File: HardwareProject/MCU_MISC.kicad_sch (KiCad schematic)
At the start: 61 parts, among them J4 Conn_ARM_JTAG_SWD_20, J5 Conn_01x03, J6 Conn_01x03, J7 SMA, J8 SMA, SW1 焊盘, SW2 Push_Button, SW3 Push_Button, SW4 Push_Button, U10 TJA1044GTK/3Z, U19 XC6206PxxxMR, U22 TMP112xxDRL, U4 HPM6P41IPB1, U6 AT24C08C-SSHM-T, U7 TMP112xxDRL, U8 TMP112xxDRL, U9 SIT3088ETK, Y1 24MHz ±10ppm 6pF

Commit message: Rev3最终版本
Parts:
- added TP5, TP6: TestPoint_Probe, HPM6P41_BB:TestPoint_Bridge_Pitch1.2mm_Drill0.7mm, symbol Connector:TestPoint_Probe
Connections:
- net 485_RX: now also TP5.1
- net 485_TX: now also TP6.1
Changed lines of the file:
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@@
 	)
 	(junction
+		(at 200.66 125.73)
+		(diameter 0)
+		(color 0 0 0 0)
+	)
+	(junction
 		(at 86.36 97.79)
 		(diameter 0)
@@
 	)
 	(junction
+		(at 200.66 115.57)
+		(diameter 0)
+		(color 0 0 0 0)
+	)
+	(junction
 		(at 78.74 138.43)
 		(diameter 0)
@@
 	(wire
 		(pts
+			(xy 200.66 127) (xy 200.66 125.73)
+		)
+		(stroke
+			(width 0)
+			(type default)
+		)
+	)
+	(wire
+		(pts
 			(xy 246.38 50.8) (xy 259.08 50.8)
 		)
@@
 	(wire
 		(pts
+			(xy 200.66 114.3) (xy 200.66 115.57)
+		)
+		(stroke
+			(width 0)
+			(type default)
+		)
+	)
+	(wire
+		(pts
 			(xy 209.55 104.14) (xy 210.82 104.14)
 		)
@@
 	)
 	(symbol
+		(lib_id "Connector:TestPoint_Probe")
+		(at 200.66 127 180)
+		(unit 1)
+		(exclude_from_sim no)
+		(in_bom yes)
+		(on_board yes)
+		(dnp no)
+		(property "Reference" "TP6"
+			(at 197.104 131.826 0)
+			(effects
+				(font
+					(size 1.27 1.27)
+				)
+				(justify right)
+			)
+		)
+		(property "Value" "TestPoint_Probe"
+			(at 196.85 127.3176 0)
+			(effects
+				(font
+					(size 1.27 1.27)
+				)
+				(justify left)
+				(hide yes)
+			)
+		)
+		(property "Footprint" "HPM6P41_BB:TestPoint_Bridge_Pitch1.2mm_Drill0.7mm"
+			(at 195.58 127 0)
+			(effects
+				(font
+					(size 1.27 1.27)
+				)
+				(hide yes)
+			)
+		)
+		(property "Datasheet" "~"
+			(at 195.58 127 0)
+			(effects
+				(font
+					(size 1.27 1.27)
+				)
+				(hide yes)
+			)
+		)
+		(property "Description" "test point (alternative probe-style design)"
+			(at 200.66 127 0)
+			(effects
+				(font
+					(size 1.27 1.27)
+				)
+				(hide yes)
+			)
+		)
+		(pin "1"
+		)
+		(instances
+			(project "HPM6P41_BB"
+				(path "/714b8a30-f9a7-49d4-a000-bc20c4884c7a/5ba70b1a-2680-42f0-98ce-27de27e994eb"
+					(reference "TP6")
+					(unit 1)
+				)
+			)
+		)
+	)
+	(symbol
 		(lib_id "power:+3.3V")
 		(at 172.72 29.21 0)
@@
 					(unit 1)
 				)
+			)
+		)
+	)
+	(symbol
+		(lib_id "Connector:TestPoint_Probe")
+		(at 200.66 114.3 90)
+		(unit 1)
+		(exclude_from_sim no)
+		(in_bom yes)
+		(on_board yes)
+		(dnp no)
+		(fields_autoplaced yes)
+		(property "Reference" "TP5"
+			(at 199.0725 109.22 90)
+			(effects
+				(font
+					(size 1.27 1.27)
+				)
+			)
+		)
+		(property "Value" "TestPoint_Probe"
+			(at 200.3424 110.49 0)
+			(effects
+				(font
+					(size 1.27 1.27)
+				)
+				(justify left)
+				(hide yes)
+			)
+		)
+		(property "Footprint" "HPM6P41_BB:TestPoint_Bridge_Pitch1.2mm_Drill0.7mm"
+			(at 200.66 109.22 0)
+			(effects
+				(font
+					(size 1.27 1.27)
+				)
+				(hide yes)
+			)
+		)
+		(property "Datasheet" "~"
+			(at 200.66 109.22 0)
+			(effects
+				(font
+					(size 1.27 1.27)
+				)
+				(hide yes)
+			)
+		)
+		(property "Description" "test point (alternative probe-style design)"
+			(at 200.66 114.3 0)
+			(effects
+				(font
+					(size 1.27 1.27)
+				)
+				(hide yes)
+			)
+		)
+		(pin "1"
+		)
+		(instances
+			(project "HPM6P41_BB"
+				(path "/714b8a30-f9a7-49d4-a000-bc20c4884c7a/5ba70b1a-2680-42f0-98ce-27de27e994eb"
+					(reference "TP5")
+					(unit 1)
+				)

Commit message: 外置核心电压SYR838以改善ADC噪声
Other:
- note added: "EEPROM JTAG TRGM 温度计"
- note removed: "USB EEPROM JTAG TRGM 温度计"
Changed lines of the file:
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@@
 		)
 	)
-	(text "USB EEPROM\nJTAG TRGM 温度计"
+	(text "EEPROM JTAG TRGM 温度计"
 		(exclude_from_sim no)
 		(at 95.504 185.42 0)

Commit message: 换其他电感之前暂存一下
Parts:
- removed C84, C85: 1uF,10V, Capacitor_SMD:C_0603_1608Metric, symbol Device:C
- removed J4: Conn_ARM_JTAG_SWD_20, Connector_IDC:IDC-Header_2x10_P2.54mm_Vertical, symbol Connector:Conn_ARM_JTAG_SWD_20
- removed TP5, TP6: TestPoint_Probe, HPM6P41_BB:TestPoint_Bridge_Pitch1.2mm_Drill0.7mm, symbol Connector:TestPoint_Probe
- removed U19: XC6206PxxxMR, Package_TO_SOT_SMD:SOT-23-3, symbol Regulator_Linear:XC6206PxxxMR
- added C100, C101: 100nF, Capacitor_SMD:C_0603_1608Metric, symbol Device:C
- added C102, C103: 4.7uF,10V, Capacitor_SMD:C_0603_1608Metric, symbol Device:C
- added U27: CA-IS3762HN, kicad_community_lib:CA-IS3762HN, symbol CA-IS3762HN:CA-IS3762HN
- added U28: TME-0505S, Converter_DCDC:Converter_DCDC_TRACO_TME_03xxS_05xxS_12xxS_Single_THT, symbol Converter_DCDC:TME-0505S
- J7, J8: footprint HPM6P41_BB:SMA_Amphenol_901-144_Vertical -> Connector_Coaxial:SMA_Amphenol_901-144_Vertical
- L2, L3: footprint 1MyFootPrint:L4532 -> HPM6P41_BB:SDCW2012-2-900TF
- U9: footprint Package_SO:SOIC-8_3.9x4.9mm_P1.27mm -> Package_SON:HVSON-8-1EP_3x3mm_P0.65mm_EP1.6x2.4mm
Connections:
- net +3.3V: now also C100.2, U27.1 (VDDA)
- net +5V: now also C102.1, U28.2 (+Vin); no longer C29.2, U10.3 (VCC)
- net 485_DE: now also U27.2 (VI1); no longer R40.2, U9.2 (~{RE}), U9.3 (DE)
- net 485_RX: now also U27.6 (VO5); no longer U9.1 (RO)
- net 485_TX: now also U27.3 (VI2); no longer U9.4 (DI)
- net CAN_RXD: now also U27.7 (VO6); no longer U10.4 (RXD)
- net CAN_STBY: now also U27.5 (VI4); no longer U10.8 (STB)
- net CAN_TXD: now also U27.4 (VI3); no longer U10.1 (TXD)
- net GND: now also C100.1, C102.2, U27.8 (GNDA), U28.1 (-Vin); no longer C27.1, C28.1, C29.1, C30.1, C31.2, C32.1, C33.2, D10.3 (A), D9.3 (A), J5.2 (Pin_2), J6.2 (Pin_2), R40.1, U10.2 (GND), U10.9 (EP), U9.5 (GND)
- net at L3.1: now also U10.6 (CANL); no longer U10.7 (CANH)
- net at L3.2: now also U10.7 (CANH); no longer U10.6 (CANL)
- net at C31.1, J5.1 (Pin_1), JP2.1 (A): now also D9.1 (K), L3.4; no longer D9.2 (K), L3.3
- net at C30.2, J5.3 (Pin_3), R42.1: now also D9.2 (K), L3.3; no longer D9.1 (K), L3.4
- net at C32.2, D10.2 (K), J6.1 (Pin_1)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: now also L2.4; no longer L2.3
- net at C33.1, D10.1 (K), J6.3 (Pin_3)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: now also L2.3; no longer L2.4
- net at L2.1: now also U9.6 (A); no longer U9.7 (B)
- net at L2.2: now also U9.7 (B); no longer U9.6 (A)
- net +3.3VC renamed +5VC
- net +5VC: now also C29.2, U10.3 (VCC), C101.2, C103.1, U27.16 (VDDB), U28.4 (+Vout)
- new net 485_DE_ISO: R40.2, U27.13 (VO3), U9.2 (~{RE}), U9.3 (DE)
- new net 485_RX_ISO: U27.10 (VI6), U9.1 (RO)
- new net 485_TX_ISO: U27.12 (VO4), U9.4 (DI)
- new net CAN_RXD_ISO: U10.4 (RXD), U27.11 (VI5)
- new net CAN_STBY_ISO: U10.8 (STB), U27.14 (VO2)
- new net CAN_TXD_ISO: U10.1 (TXD), U27.15 (VO1)
- new net ISO_GNDC: C101.1, C103.2, C27.1, C28.1, C29.1, C30.1, C31.2, C32.1, C33.2, D10.3 (A), D9.3 (A), J5.2 (Pin_2), J6.2 (Pin_2), R40.1, U10.2 (GND), U10.9 (EP), U27.9 (GNDB), U28.3 (-Vout), U9.5 (GND), U9.9 (EP)
- no-connect marks 5 -> 0
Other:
- note added: "EEPROM TRGM 温度计"
- note removed: "EEPROM JTAG TRGM 温度计"
- moved on the sheet: C23, C24, C26, C88, J7, J8, JP1, R35, R36, R38, R39, R49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

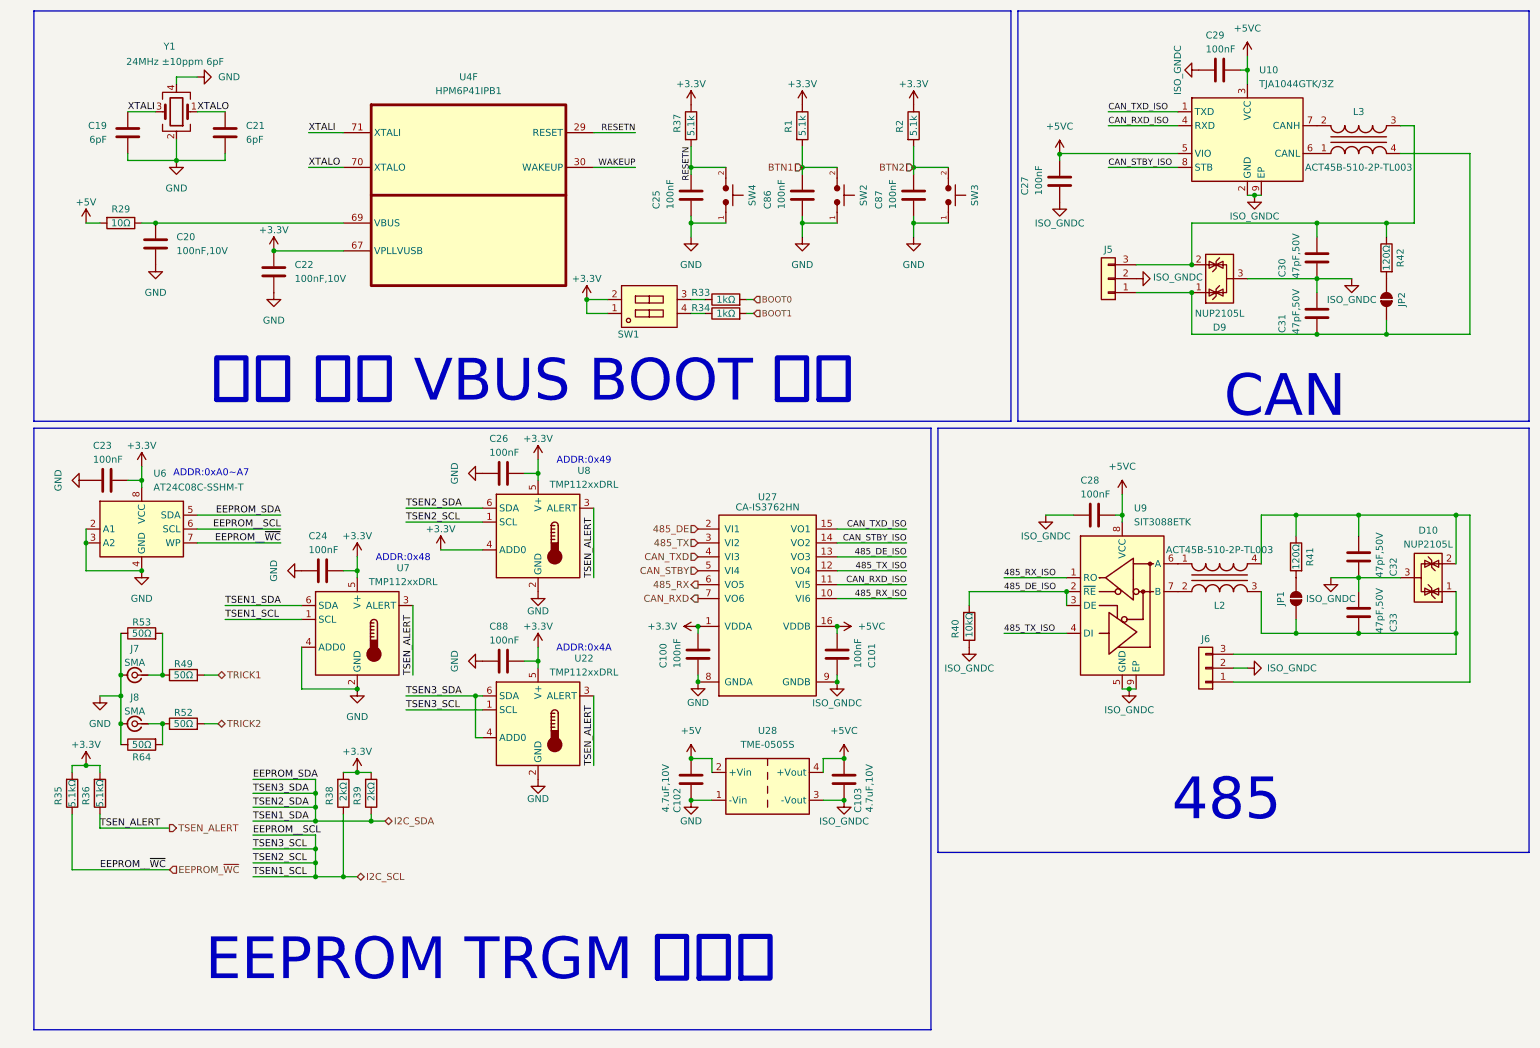
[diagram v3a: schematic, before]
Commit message: 完成Rev4 电源 驱动 模拟 IO
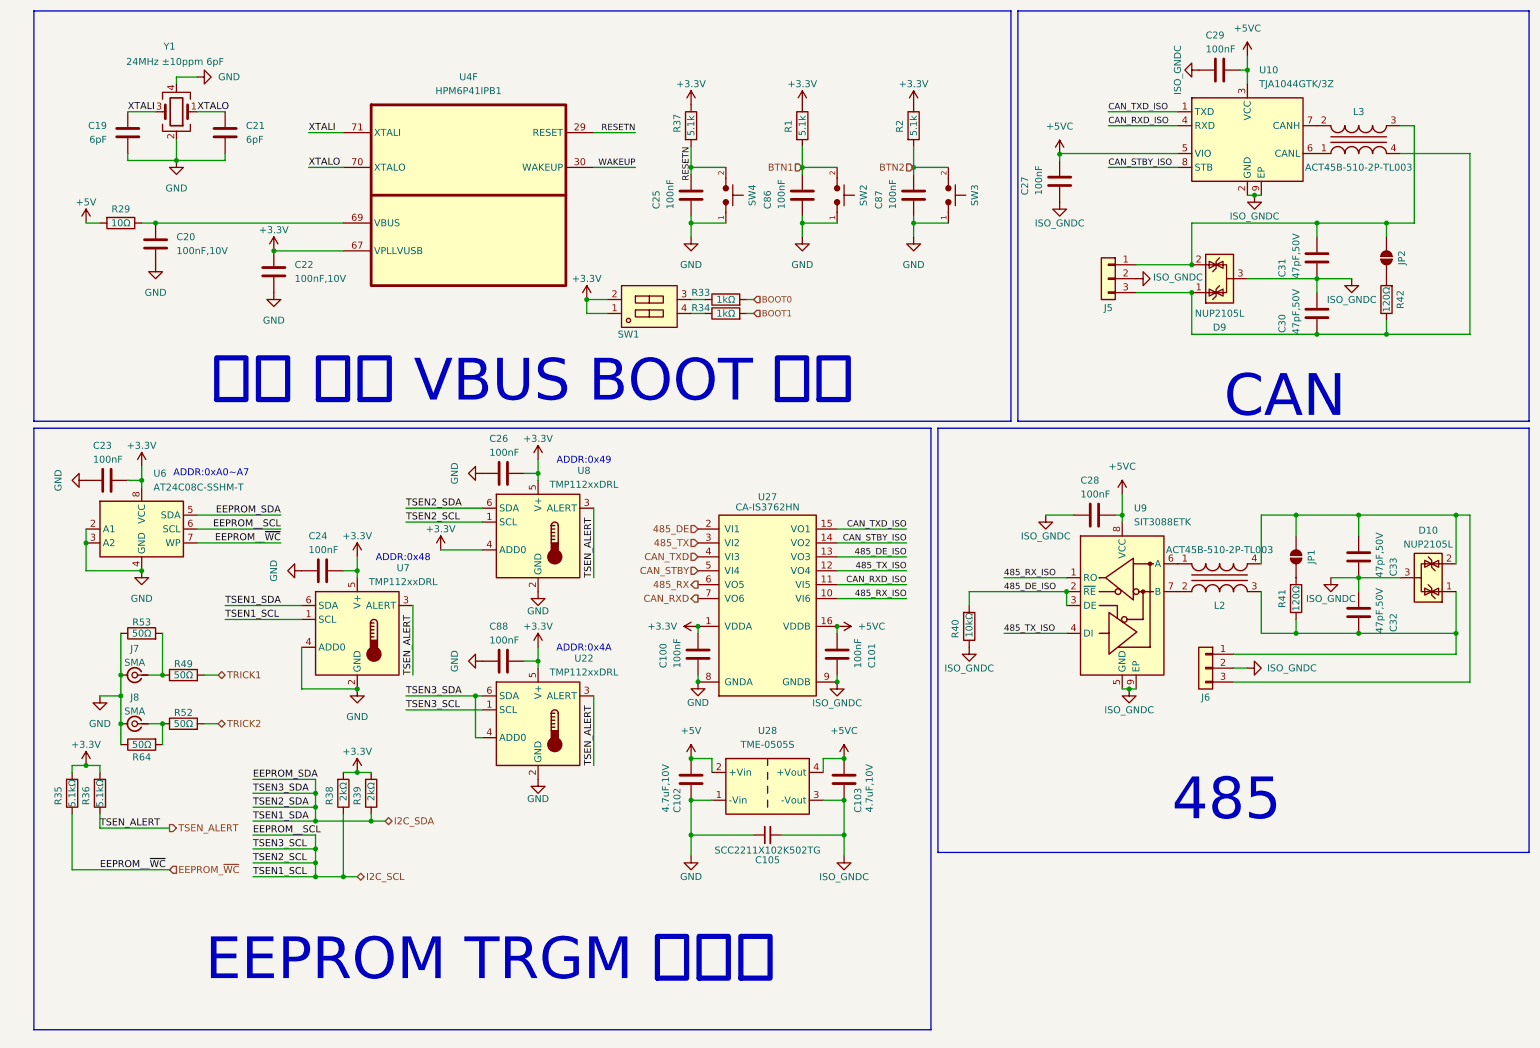
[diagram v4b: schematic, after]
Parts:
- added C105: SCC2211X102K502TG, kicad_community_lib:SCC2211X102K502T, symbol SCC2211X102K502T:SCC2211X102K502T
- J7, J8: footprint Connector_Coaxial:SMA_Amphenol_901-144_Vertical -> HPM6P41_BB:SMA_Amphenol_901-144_Vertical
- U28: footprint Converter_DCDC:Converter_DCDC_TRACO_TME_03xxS_05xxS_12xxS_Single_THT -> HPM6P41_BB:BXXXXS-1W隔离电源
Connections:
- net GND: now also C105.1
- net ISO_GNDC: now also C30.2, C31.1, C32.2, C33.1, C105.2; no longer C30.1, C31.2, C32.1, C33.2
- new net: C31.2, D9.2 (K), J5.1 (Pin_1), JP2.1 (A), L3.3
- new net: C30.1, D9.1 (K), J5.3 (Pin_3), L3.4, R42.1
- new net: C32.1, D10.1 (K), J6.1 (Pin_1), L2.3, R41.1
- new net: C33.2, D10.2 (K), J6.3 (Pin_3), JP1.1 (A), L2.4
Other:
- moved on the sheet: C30, C31, C32, C33, J5, J6, JP1, JP2, R41, R42

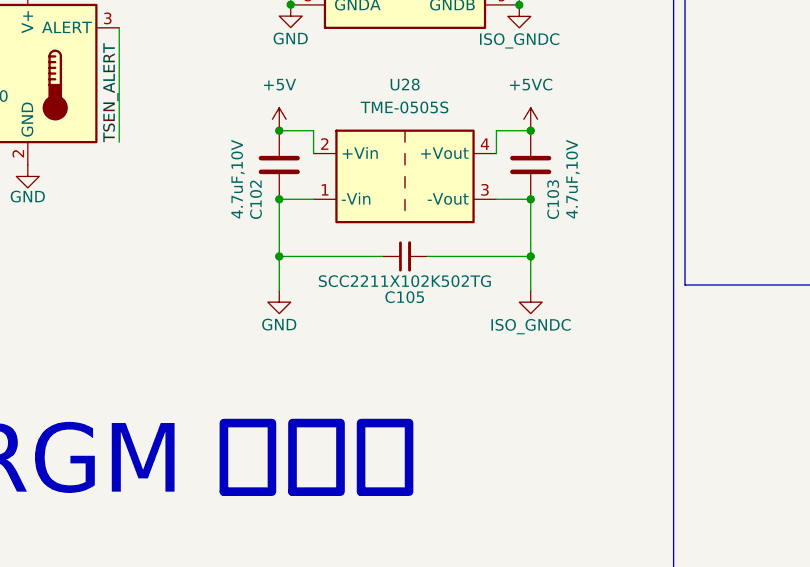
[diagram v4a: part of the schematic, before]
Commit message: 更新readme暂停通知，添加测试用例源代码
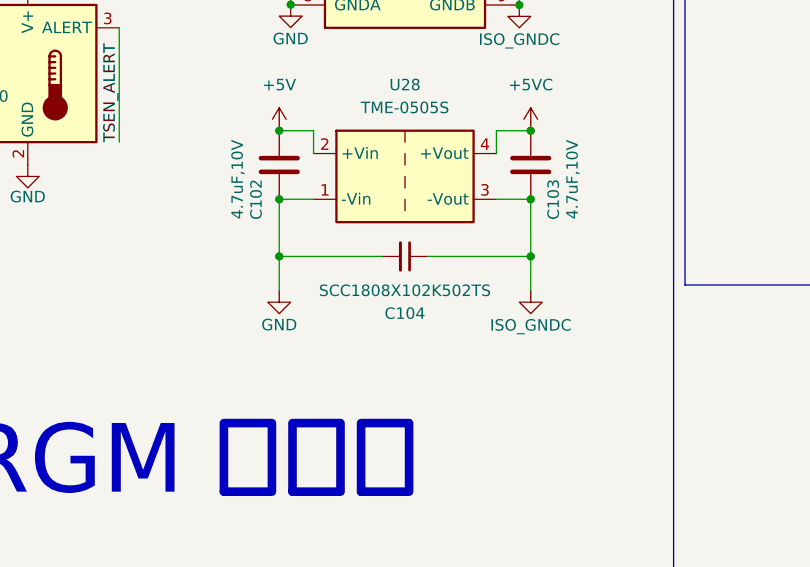
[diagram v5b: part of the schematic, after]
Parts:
- removed C105: SCC2211X102K502TG, kicad_community_lib:SCC2211X102K502T, symbol SCC2211X102K502T:SCC2211X102K502T
- added C104: SCC1808X102K502TS, Capacitor_SMD:C_1808_4520Metric, symbol SCC1808X102K502TS:SCC1808X102K502TS
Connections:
- net GND: now also C104.2
- net ISO_GNDC: now also C104.1
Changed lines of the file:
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@@
+	)
+	(symbol
+		(lib_id "SCC1808X102K502TS:SCC1808X102K502TS")
+		(at 146.05 162.56 270)
+		(mirror x)
+		(unit 1)
+		(exclude_from_sim no)
+		(in_bom yes)
+		(on_board yes)
+		(dnp no)
+		(property "Reference" "C104"
+			(at 146.0436 168.91 90)
+			(effects
+				(font
+					(size 1.27 1.27)
+				)
+			)
+		)
+		(property "Value" "SCC1808X102K502TS"
+			(at 146.0436 166.37 90)
+			(effects
+				(font
+					(size 1.27 1.27)
+				)
+			)
+		)
+		(property "Footprint" "Capacitor_SMD:C_1808_4520Metric"
+			(at 146.05 162.56 0)
+			(effects
+				(font
+					(size 1.27 1.27)
+				)
+				(hide yes)
+			)
+		)
+		(property "Datasheet" "https://file.elecfans.com/web2/M00/22/AF/poYBAGGoaTeAQmH1AAyzIp8aHB4719.pdf"
+			(at 146.05 162.56 0)
+			(effects
+				(font
+					(size 1.27 1.27)
+				)
+				(hide yes)
+			)
+		)
+		(property "Description" "Safety Capacitors 1808 1nF ±10% 250V"
+			(at 146.05 162.56 0)
+			(effects
+				(font
+					(size 1.27 1.27)
+				)
+				(hide yes)
+			)
+		)
+		(property "MPN" "SCC1808X102K502TS"
+			(at 146.05 162.56 0)
+			(effects
+				(font
+					(size 1.27 1.27)
+				)
+				(hide yes)
+			)
+		)
+		(property "Manufacturer" "IHHEC"
+			(at 146.05 162.56 0)
+			(effects
+				(font
+					(size 1.27 1.27)
+				)
+				(hide yes)
+			)
+		)
+		(property "Grade" "X1,Y2"
+			(at 146.05 162.56 0)
+			(effects
+				(font
+					(size 1.27 1.27)
+				)
+				(hide yes)
+			)
+		)
+		(property "MFG" "IHHEC"
+			(at 146.05 162.56 0)
+			(effects
+				(font
+					(size 1.27 1.27)
+				)
+				(hide yes)
+			)
+		)
+		(property "MFR Package Code" "1808"
+			(at 146.05 162.56 0)
+			(effects
+				(font
+					(size 1.27 1.27)
+				)
+				(hide yes)
+			)
+		)
+		(property "Mount" "表面贴装"
+			(at 146.05 162.56 0)
+			(effects
+				(font
+					(size 1.27 1.27)
+				)
+				(hide yes)
+			)
+		)
+		(property "Operating Temperature" "-55 °C"
+			(at 146.05 162.56 0)
+			(effects
+				(font
+					(size 1.27 1.27)
+				)
+				(hide yes)
+			)
+		)
+		(property "Tolerance" "10 %"
+			(at 146.05 162.56 0)
+			(effects
+				(font
+					(size 1.27 1.27)
+				)
+				(hide yes)
+			)
+		)
+		(property "packaging" "1000pcs"
+			(at 146.05 162.56 0)
+			(effects
+				(font
+					(size 1.27 1.27)
+				)
+				(hide yes)
+			)
+		)
+		(pin "2"
+		)
+		(pin "1"
+		)
+		(instances
+			(project "HPM6P41_BB"
+				(path "/714b8a30-f9a7-49d4-a000-bc20c4884c7a/5ba70b1a-2680-42f0-98ce-27de27e994eb"
+					(reference "C104")
+					(unit 1)
+				)
+			)
+		)
 	)
 	(symbol
@@
 					(unit 1)
 				)
-			)
-		)
-	)
-	(symbol
-		(lib_id "SCC2211X102K502T:SCC2211X102K502T")
-		(at 146.05 162.56 90)
-		(mirror x)
-		(unit 1)
-		(exclude_from_sim no)
-		(in_bom yes)
-		(on_board yes)
-		(dnp no)
-		(property "Reference" "C105"
-			(at 146.05 167.132 90)
-			(effects
-				(font
-					(size 1.27 1.27)
-				)
-			)
-		)
-		(property "Value" "SCC2211X102K502TG"
-			(at 146.05 165.354 90)
-			(effects
-				(font
-					(size 1.27 1.27)
-				)
-			)
-		)
-		(property "Footprint" "kicad_community_lib:SCC2211X102K502T"
-			(at 146.05 162.56 0)
-			(effects
-				(font
-					(size 1.27 1.27)
-				)
-				(hide yes)
-			)
-		)
-		(property "Datasheet" ""
-			(at 146.05 162.56 0)
-			(effects
-				(font
-					(size 1.27 1.27)
-				)
-				(hide yes)
-			)
-		)
-		(property "Description" "Safety Capacitors 2211 1nF ±10% 250V"
-			(at 146.05 162.56 0)
-			(effects
-				(font
-					(size 1.27 1.27)
-				)
-				(hide yes)
-			)
-		)
-		(property "Mpn" "SCC2211X102K502T"
-			(at 146.05 162.56 0)
-			(effects
-				(font
-					(size 1.27 1.27)
-				)
-				(hide yes)
-			)
-		)
-		(property "Manufacturer" "IHHEC"
-			(at 146.05 162.56 0)
-			(effects
-				(font
-					(size 1.27 1.27)
-				)
-				(hide yes)
-			)
-		)
-		(property "Mount" "表面贴装"
-			(at 146.05 162.56 0)
-			(effects
-				(font
-					(size 1.27 1.27)
-				)
-				(hide yes)
-			)
-		)
-		(property "Tolerance" "10 %"
-			(at 146.05 162.56 0)
-			(effects
-				(font
-					(size 1.27 1.27)
-				)
-				(hide yes)
-			)
-		)
-		(pin "1"
-		)
-		(pin "2"
-		)
-		(instances
-			(project "HPM6P41_BB"
-				(path "/714b8a30-f9a7-49d4-a000-bc20c4884c7a/5ba70b1a-2680-42f0-98ce-27de27e994eb"
-					(reference "C105")
-					(unit 1)
-				)
